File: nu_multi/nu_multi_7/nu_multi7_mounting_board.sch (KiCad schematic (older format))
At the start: 15 parts, among them J1 CONN_01X02, J10 CONN_01X03, J11 CONN_01X02, J12 CONN_01X03, J13 CONN_01X02, J14 CONN_01X03, J15 CONN_01X14, J2 CONN_01X03, J3 CONN_01X02, J4 CONN_01X02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

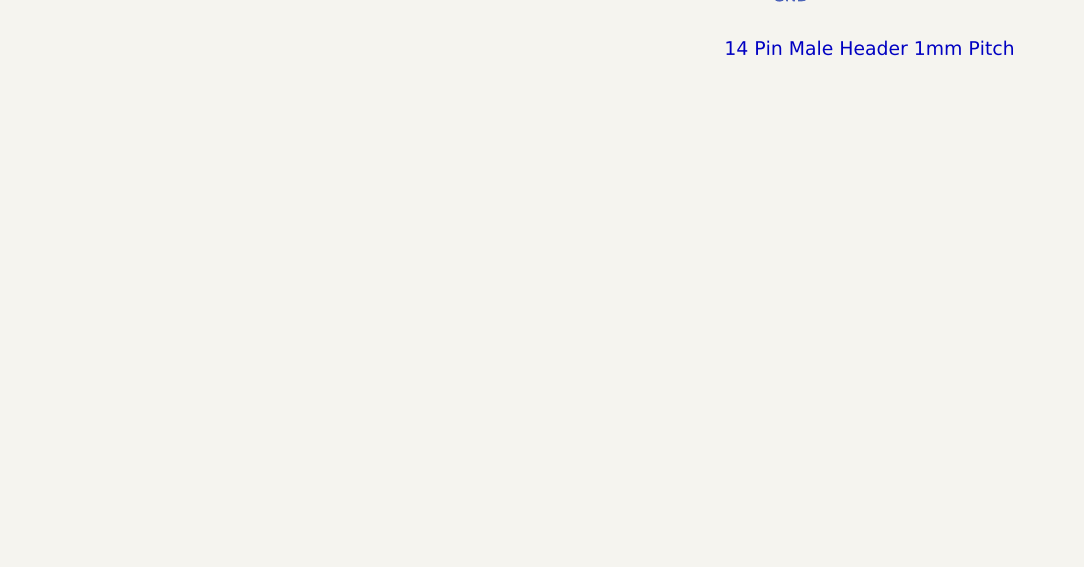
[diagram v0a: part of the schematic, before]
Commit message: Updates; added nu multi-8 mounting board
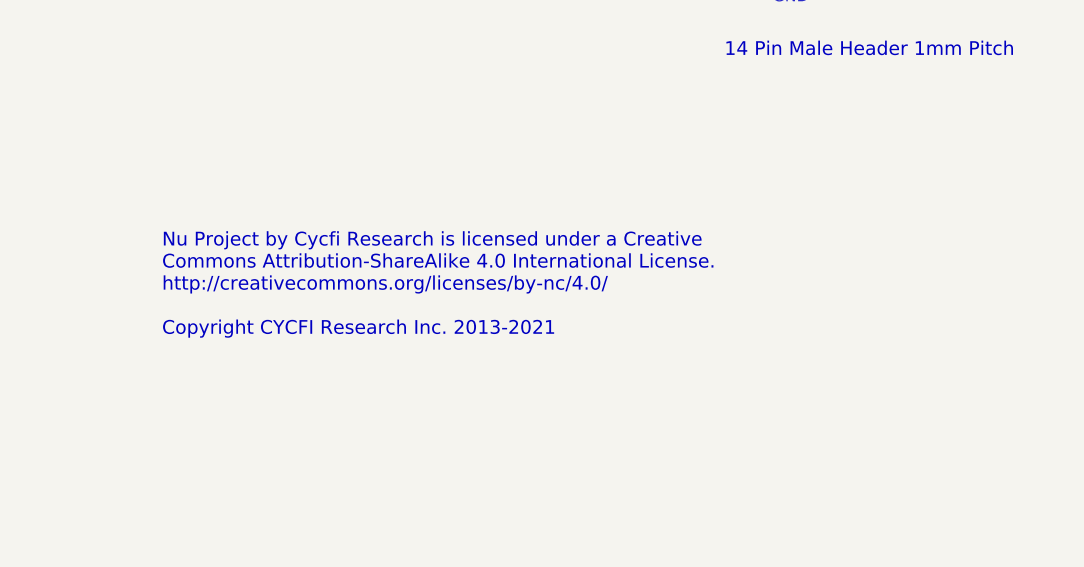
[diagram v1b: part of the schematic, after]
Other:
- note added: "Nu Project by Cycfi Research is licensed under a Creative \nCommons Attribution-ShareAlike 4.0 International License. \nhttp://creativecommons.org/licenses/by-nc/4.0/\n\nCopyright CYCFI Research Inc. 2013-2021"
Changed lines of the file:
@@
 Sheet 1 1
 Title "Nu Multi 7 Board"
-Date ""
-Rev "v0.9"
-Comp ""
+Date "2021-11-15"
+Rev "v2.5"
+Comp "Document Number: 2021010"
 Comment1 ""
 Comment2 ""
@@
 	9735 3650 9735 3750
 Connection ~ 9735 3750
+Text Notes 6985 5660 0    60   ~ 0
+Nu Project by Cycfi Research is licensed under a Creative \nCommons Attribution-ShareAlike 4.0 International License. \nhttp://creativecommons.org/licenses/by-nc/4.0/\n\nCopyright CYCFI Research Inc. 2013-2021
 $EndSCHEMATC
